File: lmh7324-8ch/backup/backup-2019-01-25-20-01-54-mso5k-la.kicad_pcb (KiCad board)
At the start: 4 copper layers, 155 parts, among them IC201 lmh7324, IC301 lmh7324, IC401 lmh7324, IC501 lmh7324, J101 output, J102 input

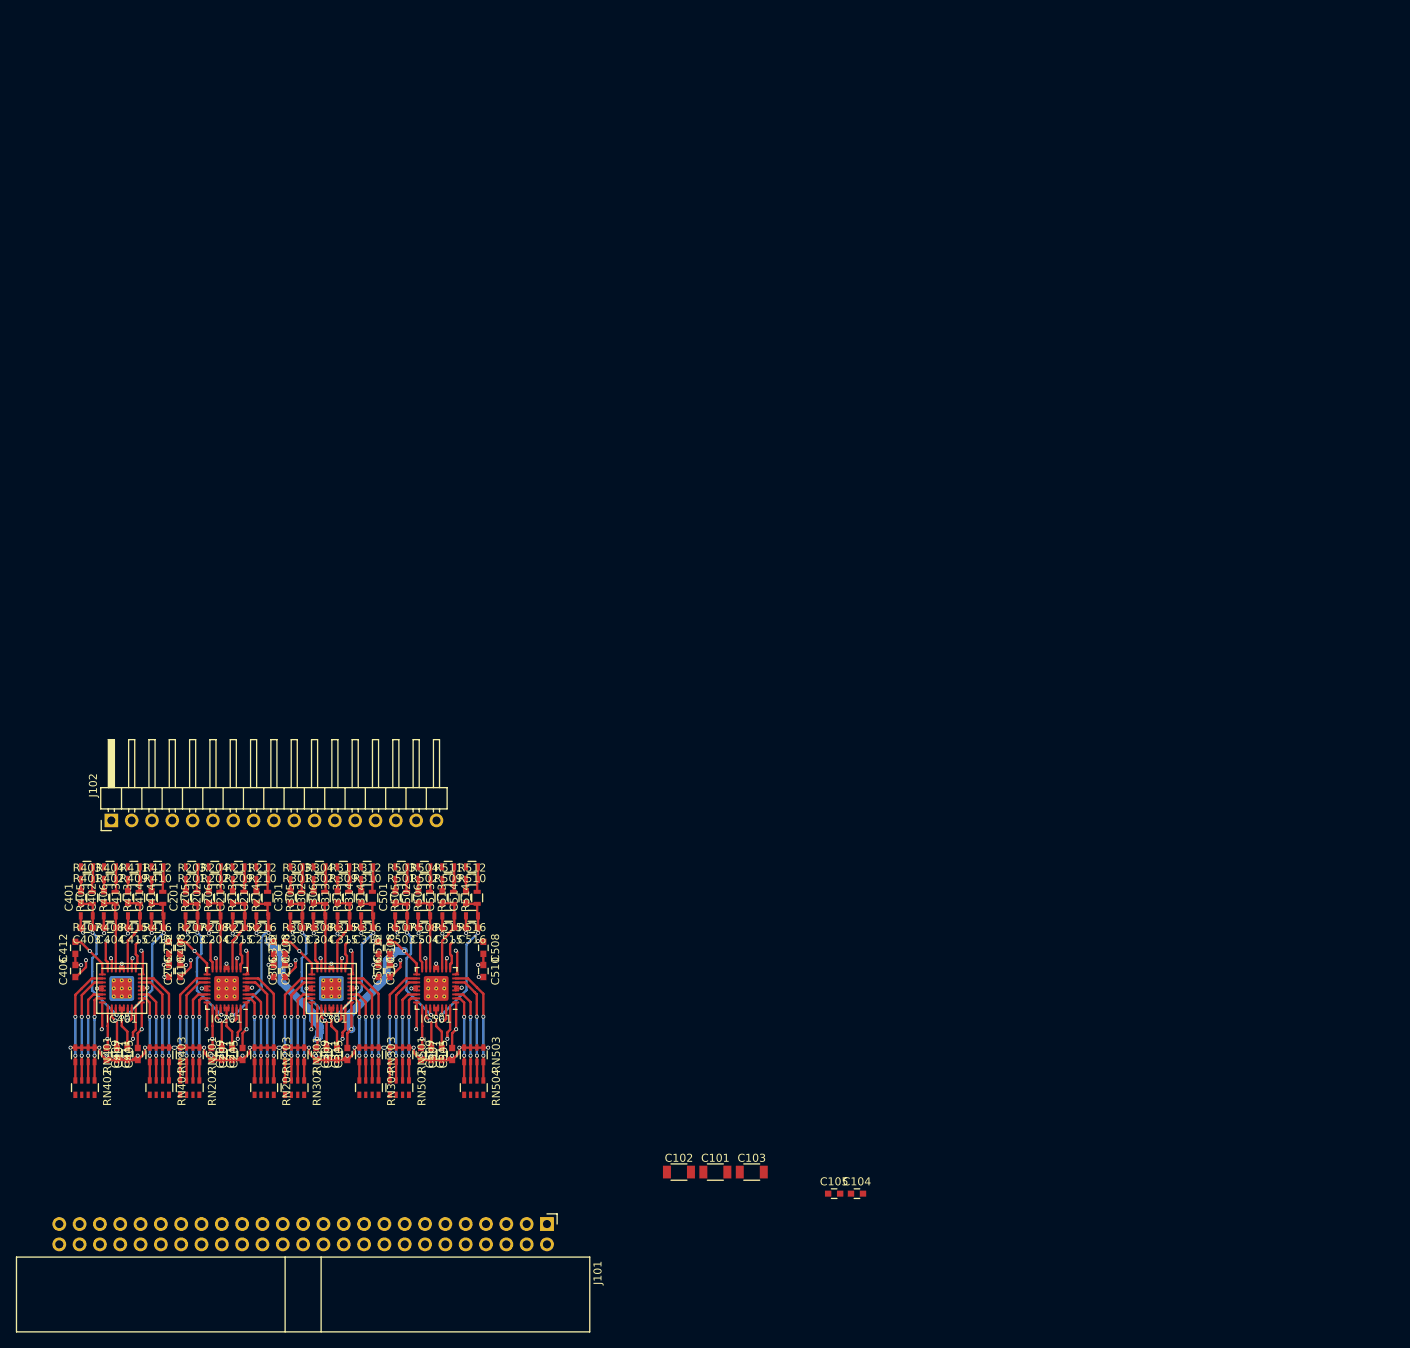
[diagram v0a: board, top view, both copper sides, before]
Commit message: Laid out the 8ch LMH7324 version and added a threshold display too
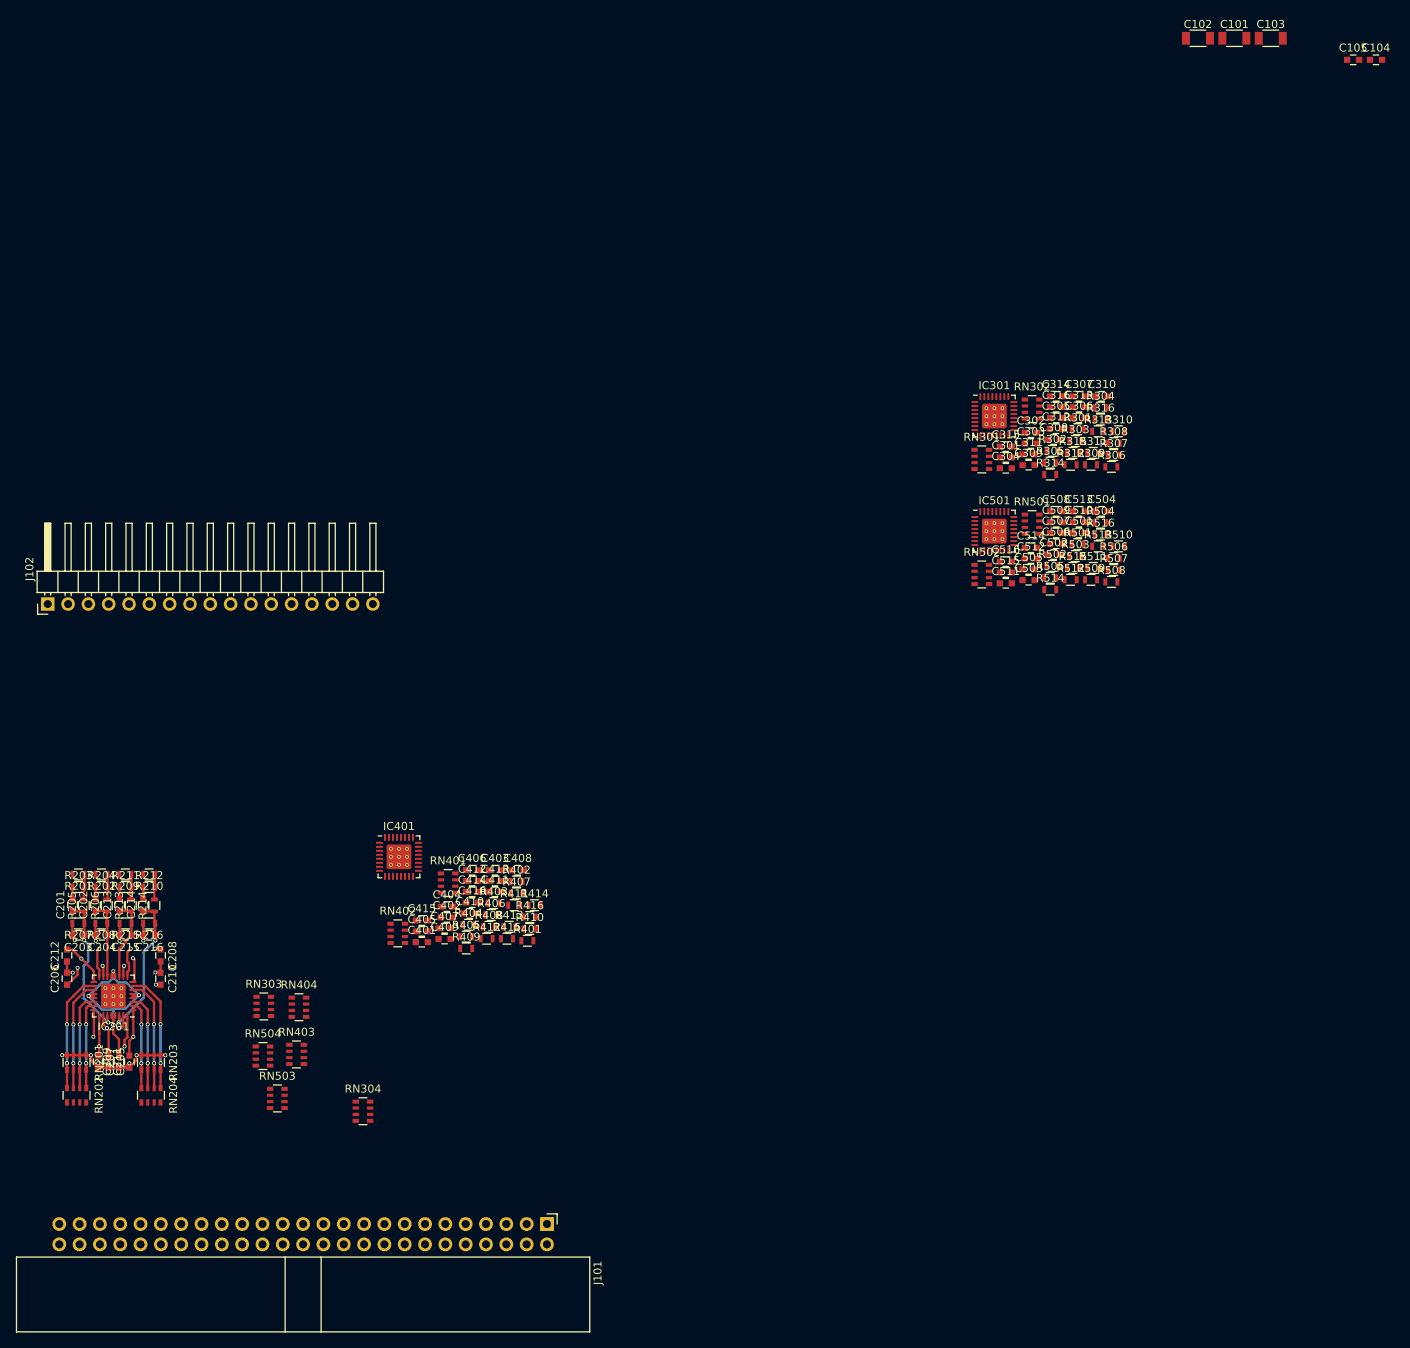
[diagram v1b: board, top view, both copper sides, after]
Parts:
- moved C101 155.9 mm to (197.5, 48.7)
- moved C102 155.9 mm to (193.0, 48.7)
- moved C103 155.9 mm to (202.1, 48.7)
- moved C104 155.9 mm to (215.2, 51.4)
- moved C105 155.9 mm to (212.4, 51.4)
- moved C307 125.9 mm to (178.1, 93.4), turned to 0 degrees
- moved RN302 125.3 mm to (172.2, 95.0), turned to 0 degrees
- moved C305 121.0 mm to (175.2, 96.1), turned to 0 degrees
- moved C306 121.0 mm to (178.1, 96.1), turned to 0 degrees
- moved R307 117.3 mm to (182.4, 100.8), turned to 0 degrees
- moved C312 116.2 mm to (175.2, 97.5), turned to 0 degrees
- moved R308 115.5 mm to (182.4, 99.3), turned to 0 degrees
- moved C310 115.5 mm to (180.9, 93.4), turned to 0 degrees
- moved R304 114.1 mm to (180.8, 94.9)
- moved RN301 113.7 mm to (166.0, 101.3), turned to 0 degrees
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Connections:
- IC301 pad 11: Net-(C313-Pad1) -> Net-(C302-Pad1)
- IC301 pad 14: Net-(C302-Pad1) -> Net-(C313-Pad1)
- IC301 pad 18: /Ch 8-11/B- -> /Ch 8-11/C-
- IC301 pad 19: /Ch 8-11/B+ -> /Ch 8-11/C+
- IC301 pad 2: /Ch 8-11/D- -> /Ch 8-11/A-
- IC301 pad 22: /Ch 8-11/A+ -> /Ch 8-11/D+
- IC301 pad 23: /Ch 8-11/A- -> /Ch 8-11/D-
- IC301 pad 27: Net-(C301-Pad1) -> Net-(C314-Pad1)
- IC301 pad 3: /Ch 8-11/D+ -> /Ch 8-11/A+
- IC301 pad 30: Net-(C314-Pad1) -> Net-(C301-Pad1)
- IC301 pad 6: /Ch 8-11/C+ -> /Ch 8-11/B+
- IC301 pad 7: /Ch 8-11/C- -> /Ch 8-11/B-
- IC401 pad 11: Net-(C413-Pad1) -> Net-(C402-Pad1)
- IC401 pad 14: Net-(C402-Pad1) -> Net-(C413-Pad1)
- IC401 pad 18: /Ch 0-3/B- -> /Ch 0-3/C-
- IC401 pad 19: /Ch 0-3/B+ -> /Ch 0-3/C+
- IC401 pad 2: /Ch 0-3/D- -> /Ch 0-3/A-
- IC401 pad 22: /Ch 0-3/A+ -> /Ch 0-3/D+
- IC401 pad 23: /Ch 0-3/A- -> /Ch 0-3/D-
- IC401 pad 27: Net-(C401-Pad1) -> Net-(C414-Pad1)
- IC401 pad 3: /Ch 0-3/D+ -> /Ch 0-3/A+
- IC401 pad 30: Net-(C414-Pad1) -> Net-(C401-Pad1)
- IC401 pad 6: /Ch 0-3/C+ -> /Ch 0-3/B+
- IC401 pad 7: /Ch 0-3/C- -> /Ch 0-3/B-
- IC501 pad 11: Net-(C513-Pad1) -> Net-(C502-Pad1)
- IC501 pad 14: Net-(C502-Pad1) -> Net-(C513-Pad1)
- IC501 pad 18: /12-15/B- -> /12-15/C-
- IC501 pad 19: /12-15/B+ -> /12-15/C+
- IC501 pad 2: /12-15/D- -> /12-15/A-
- IC501 pad 22: /12-15/A+ -> /12-15/D+
- IC501 pad 23: /12-15/A- -> /12-15/D-
- IC501 pad 27: Net-(C501-Pad1) -> Net-(C514-Pad1)
- IC501 pad 3: /12-15/D+ -> /12-15/A+
- IC501 pad 30: Net-(C514-Pad1) -> Net-(C501-Pad1)
- IC501 pad 6: /12-15/C+ -> /12-15/B+
- IC501 pad 7: /12-15/C- -> /12-15/B-
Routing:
- net GND: track 275.5 -> 68.9 mm, vias 52 -> 13
- net +2V5: track 192.5 -> 44.8 mm, vias 16 -> 4
- net +4V: track 189.7 -> 43.7 mm, vias 20 -> 5
- net -2V5: track 142.0 -> 50.1 mm, vias 24 -> 6
- net Vref_8-15: track 72.0 -> 0.00 mm, vias 10 -> 0
- net Vref_0-7: track 69.3 -> 40.3 mm, vias 10 -> 5
- net Net-(C314-Pad1): track 18.2 -> 0.00 mm, vias 2 -> 0
- net Net-(C414-Pad1): track 18.2 -> 0.00 mm, vias 2 -> 0
- net Net-(C514-Pad1): track 18.2 -> 0.00 mm, vias 2 -> 0
- net Net-(C301-Pad1): track 18.0 -> 0.00 mm, vias 2 -> 0
- net Net-(C401-Pad1): track 18.0 -> 0.00 mm, vias 2 -> 0
- net Net-(C501-Pad1): track 18.0 -> 0.00 mm, vias 2 -> 0
- net /12-15/C-: track 15.1 -> 0.00 mm, vias 2 -> 0
- net /Ch 8-11/C-: track 15.1 -> 0.00 mm, vias 2 -> 0
- net /Ch 0-3/C-: track 15.1 -> 0.00 mm, vias 2 -> 0
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- removed copper zone on 3_Misc, net -2V5
